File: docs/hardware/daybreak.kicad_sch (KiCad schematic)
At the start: 14 parts, among them J1 Arduino UNO Q, M1 N20 lock motor A, M2 N20 lock motor B, SW1 Override button, SW2 Talk button, SW3 Phone bay microswitch, SW4 Lid reed switch, U1 DS3231 RTC (0x68), U2 BH1750 lux (0x23), U3 MPU6050 motion (0x69, AD0 hig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, U4 GUVA-S12SD UV, U5 Phototransistor (flicker, opt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, U6 DRV8833 dual motor driver

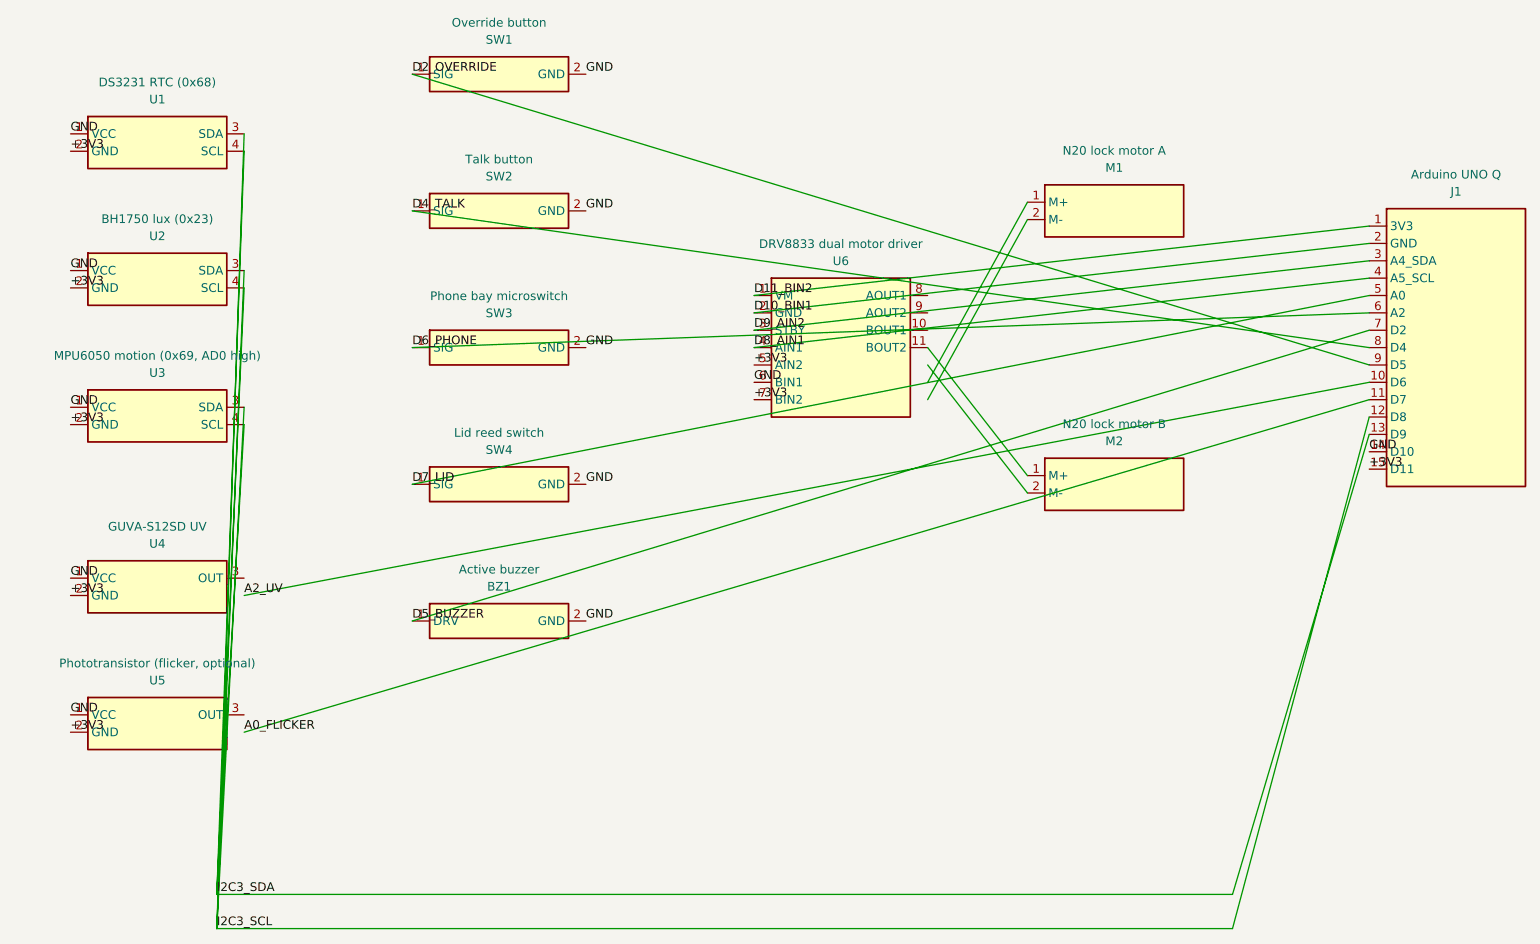
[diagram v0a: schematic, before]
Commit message: Clean up schematic net routing and add a PDF export
Switch the host fan-out (switches, buzzer, motor driver control
lines, analog sensors) to matching net labels instead of long
point-to-point wires, which was turning into a tangle. Also render
the sheet to docs/hardware/daybreak.pdf for quick viewing without
KiCad installed.
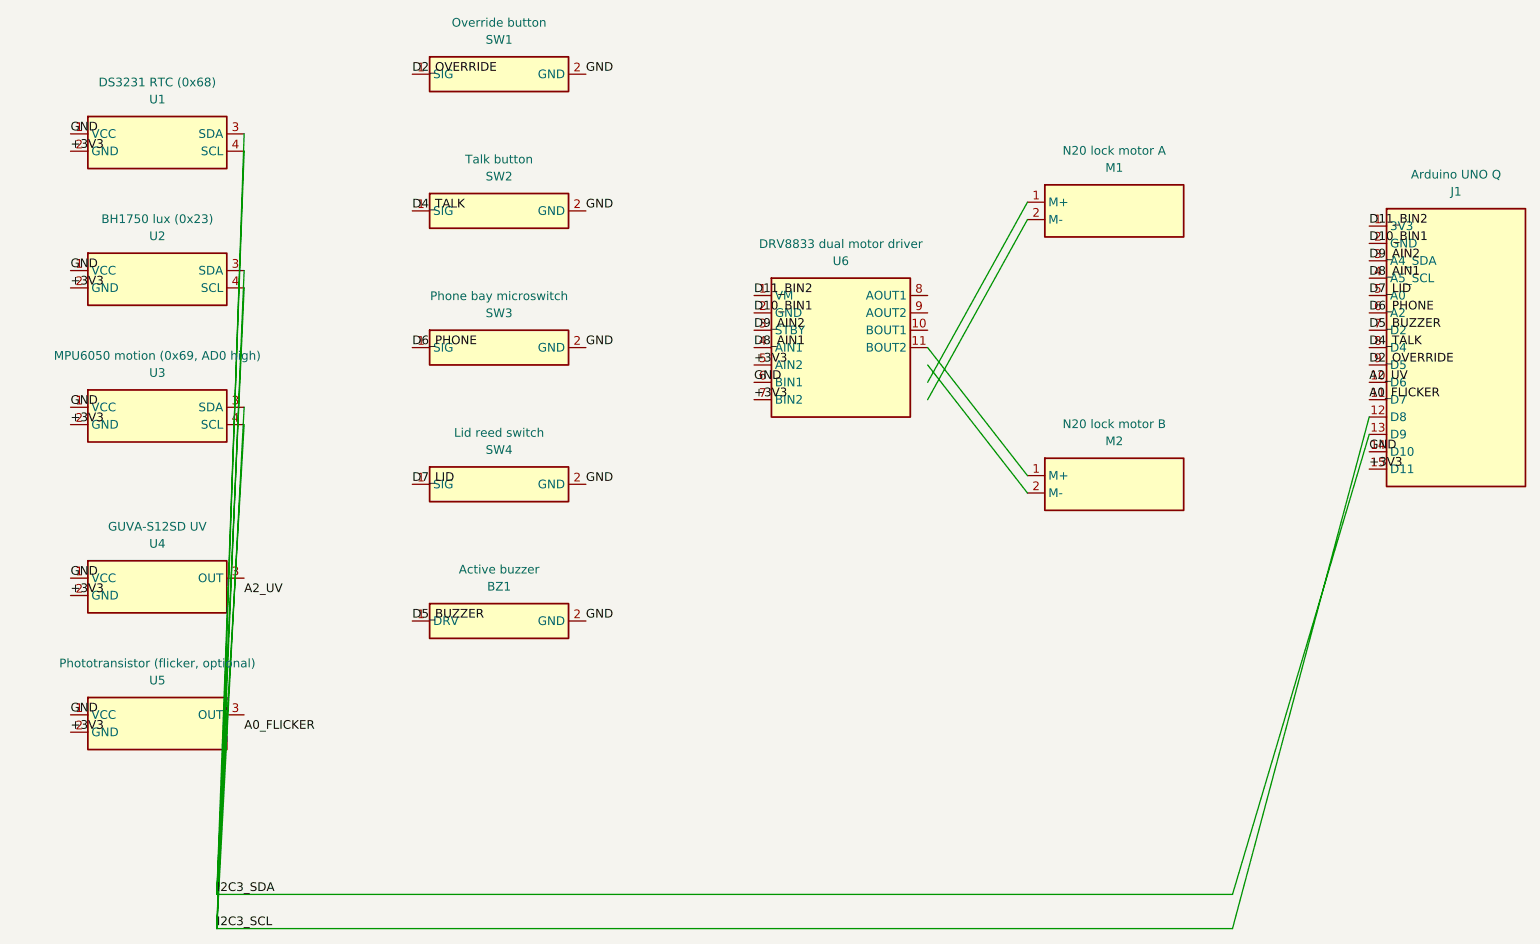
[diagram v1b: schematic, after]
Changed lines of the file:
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@@
   (wire (pts (xy 217.3 140) (xy 237.3 72.69999999999999)) (stroke (width 0) (type default)))
   (wire (pts (xy 217.3 145) (xy 237.3 70.16)) (stroke (width 0) (type default)))
-  (wire (pts (xy 72.7 96.27) (xy 237.3 65.08)) (stroke (width 0) (type default)))
-  (wire (pts (xy 72.7 116.27) (xy 237.3 67.61999999999999)) (stroke (width 0) (type default)))
-  (wire (pts (xy 97.3 20.0) (xy 237.3 62.53999999999999)) (stroke (width 0) (type default)))
-  (wire (pts (xy 97.3 40.0) (xy 237.3 59.99999999999999)) (stroke (width 0) (type default)))
-  (wire (pts (xy 97.3 60.0) (xy 237.3 54.919999999999995)) (stroke (width 0) (type default)))
-  (wire (pts (xy 97.3 80.0) (xy 237.3 52.379999999999995)) (stroke (width 0) (type default)))
-  (wire (pts (xy 97.3 100.0) (xy 237.3 57.459999999999994)) (stroke (width 0) (type default)))
-  (wire (pts (xy 147.3 60.0) (xy 237.3 49.83999999999999)) (stroke (width 0) (type default)))
-  (wire (pts (xy 147.3 57.459999999999994) (xy 237.3 47.29999999999999)) (stroke (width 0) (type default)))
-  (wire (pts (xy 147.3 54.919999999999995) (xy 237.3 44.75999999999999)) (stroke (width 0) (type default)))
-  (wire (pts (xy 147.3 52.379999999999995) (xy 237.3 42.21999999999999)) (stroke (width 0) (type default)))
   (wire (pts (xy 172.7 67.61999999999999) (xy 187.3 41.27)) (stroke (width 0) (type default)))
   (wire (pts (xy 172.7 65.08) (xy 187.3 38.730000000000004)) (stroke (width 0) (type default)))
@@
   (label "I2C3_SCL" (at 68.7 145 0) (effects (font (size 1.27 1.27)) (justify left bottom)))
   (label "A2_UV" (at 72.7 96.27 0) (effects (font (size 1.27 1.27)) (justify left bottom)))
+  (label "A2_UV" (at 237.3 65.08 0) (effects (font (size 1.27 1.27)) (justify left bottom)))
   (label "A0_FLICKER" (at 72.7 116.27 0) (effects (font (size 1.27 1.27)) (justify left bottom)))
+  (label "A0_FLICKER" (at 237.3 67.61999999999999 0) (effects (font (size 1.27 1.27)) (justify left bottom)))
   (label "D2_OVERRIDE" (at 97.3 20.0 0) (effects (font (size 1.27 1.27)) (justify left bottom)))
+  (label "D2_OVERRIDE" (at 237.3 62.53999999999999 0) (effects (font (size 1.27 1.27)) (justify left bottom)))
   (label "D4_TALK" (at 97.3 40.0 0) (effects (font (size 1.27 1.27)) (justify left bottom)))
+  (label "D4_TALK" (at 237.3 59.99999999999999 0) (effects (font (size 1.27 1.27)) (justify left bottom)))
   (label "D6_PHONE" (at 97.3 60.0 0) (effects (font (size 1.27 1.27)) (justify left bottom)))
+  (label "D6_PHONE" (at 237.3 54.919999999999995 0) (effects (font (size 1.27 1.27)) (justify left bottom)))
   (label "D7_LID" (at 97.3 80.0 0) (effects (font (size 1.27 1.27)) (justify left bottom)))
+  (label "D7_LID" (at 237.3 52.379999999999995 0) (effects (font (size 1.27 1.27)) (justify left bottom)))
   (label "D5_BUZZER" (at 97.3 100.0 0) (effects (font (size 1.27 1.27)) (justify left bottom)))
+  (label "D5_BUZZER" (at 237.3 57.459999999999994 0) (effects (font (size 1.27 1.27)) (justify left bottom)))
   (label "D8_AIN1" (at 147.3 60.0 0) (effects (font (size 1.27 1.27)) (justify left bottom)))
+  (label "D8_AIN1" (at 237.3 49.83999999999999 0) (effects (font (size 1.27 1.27)) (justify left bottom)))
   (label "D9_AIN2" (at 147.3 57.459999999999994 0) (effects (font (size 1.27 1.27)) (justify left bottom)))
+  (label "D9_AIN2" (at 237.3 47.29999999999999 0) (effects (font (size 1.27 1.27)) (justify left bottom)))
   (label "D10_BIN1" (at 147.3 54.919999999999995 0) (effects (font (size 1.27 1.27)) (justify left bottom)))
+  (label "D10_BIN1" (at 237.3 44.75999999999999 0) (effects (font (size 1.27 1.27)) (justify left bottom)))
   (label "D11_BIN2" (at 147.3 52.379999999999995 0) (effects (font (size 1.27 1.27)) (justify left bottom)))
+  (label "D11_BIN2" (at 237.3 42.21999999999999 0) (effects (font (size 1.27 1.27)) (justify left bottom)))
   (label "+3V3" (at 47.300000000000004 31.270000000000003 0) (effects (font (size 1.27 1.27)) (justify left bottom)))
   (label "+3V3" (at 47.300000000000004 51.27 0) (effects (font (size 1.27 1.27)) (justify left bottom)))
